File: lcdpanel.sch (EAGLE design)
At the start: 28 parts, among them CON1 AVRISP-NEWSYMBOL-ML6, J1 CHARLCD-LONG, SW1 PUSHSW, SW2 PUSHSW, SW3 PUSHSW, SW4 PUSHSW, U1 ATTINY2313P

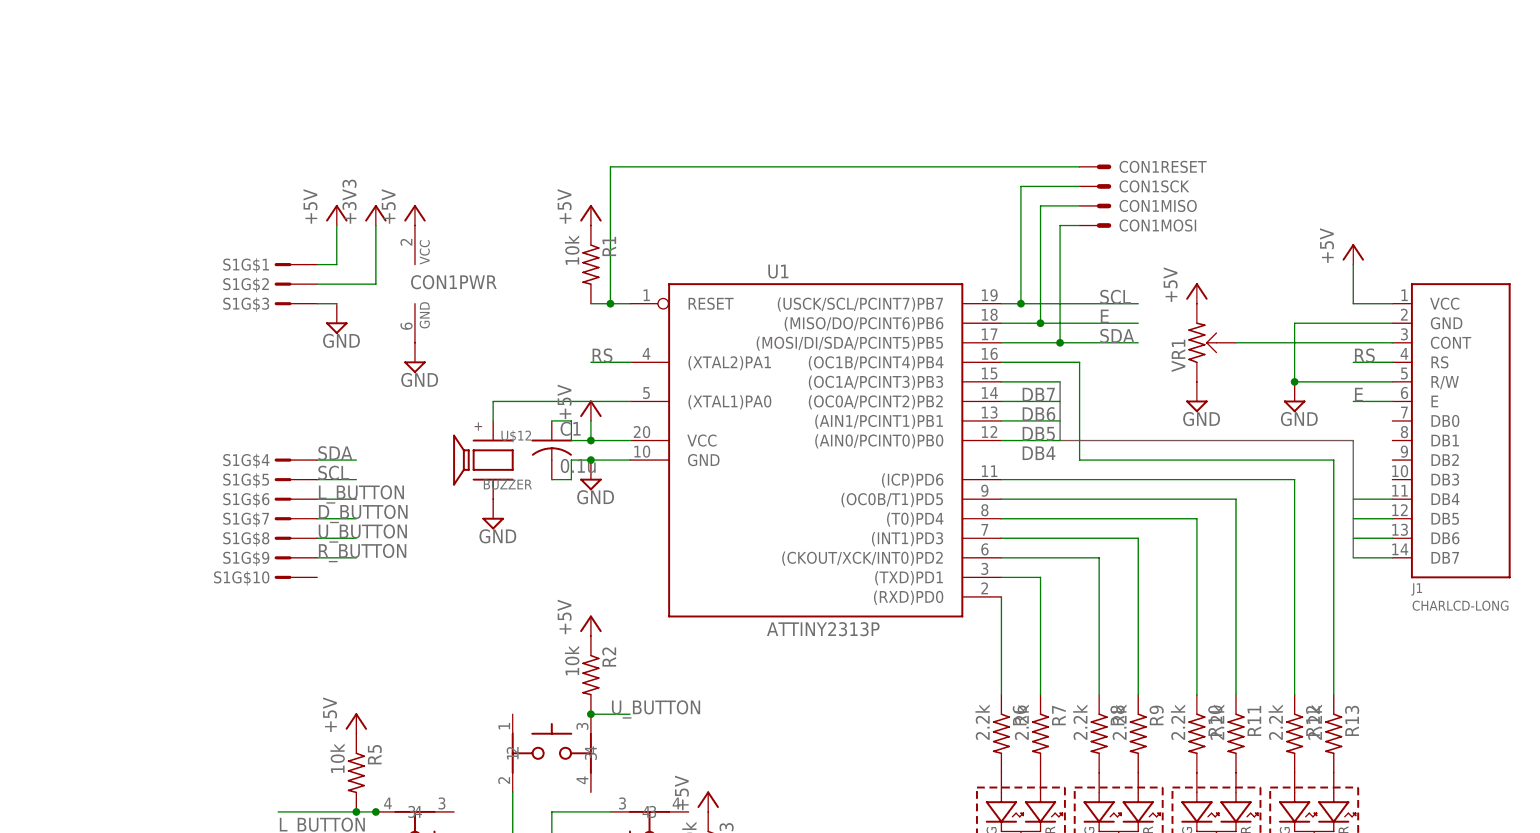
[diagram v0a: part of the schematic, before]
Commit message: added top board (ontheway)
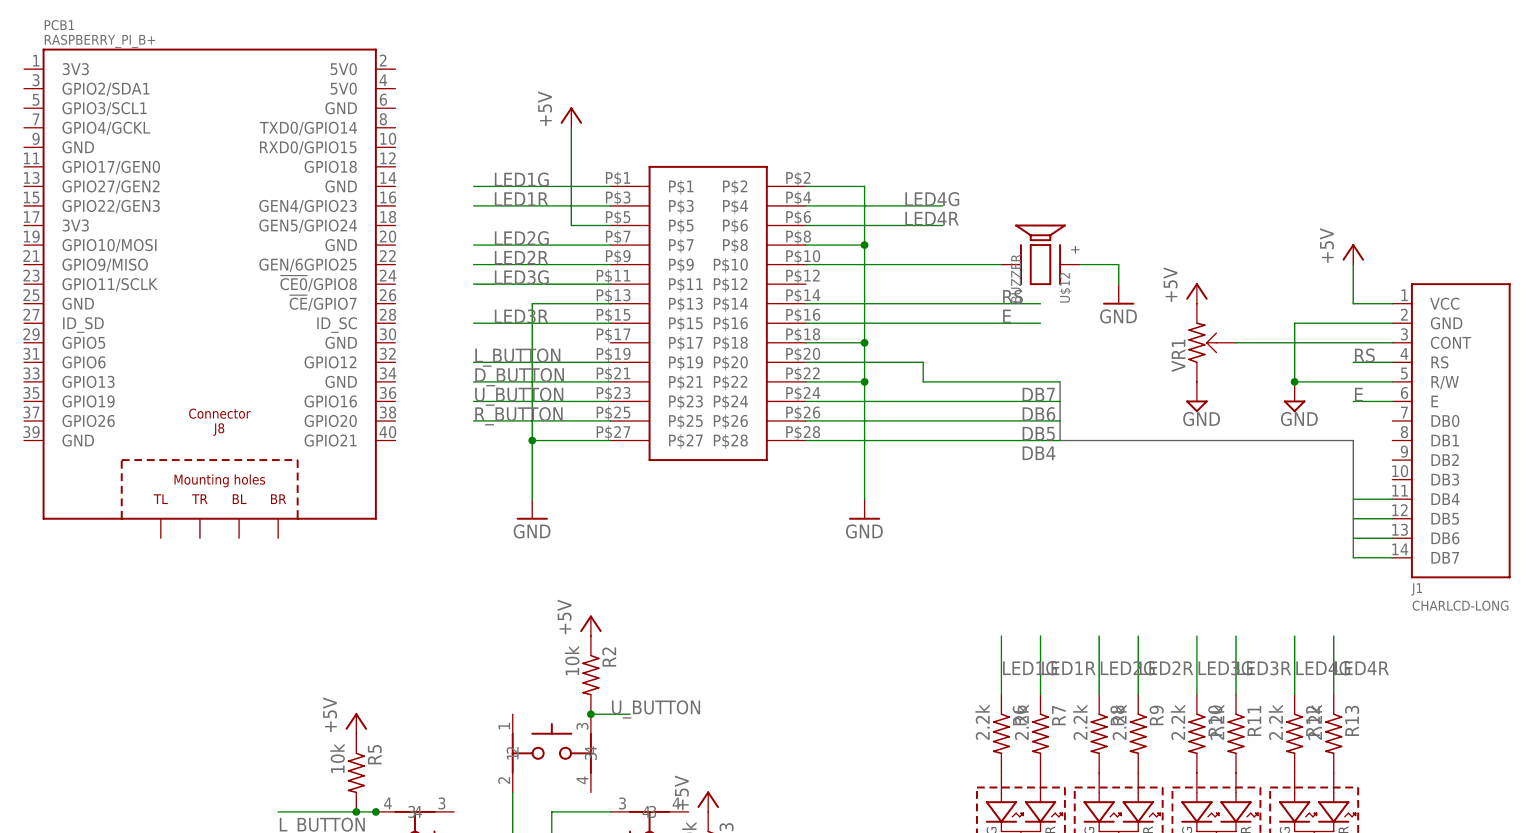
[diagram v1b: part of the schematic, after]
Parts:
- removed C1: 0.1u, Passive_Robotech:C-2012
- removed CON1: AVRISP-NEWSYMBOL-ML6, Connector_Robotech:AVRISP-NEWSYMBOL-ML6
- removed R1: 10k, Passive_Robotech:R-1608
- removed S1: 10B-PH, con-jst:10B-PH
- removed U1: ATTINY2313P, MicroControler_Robotech:ATTINY2313P
- added PCB1: RASPBERRY_PI_B+, RASPBERRY_PI_Bplus:RASPBERRY_PI_B+
- added U$13: CON_14X2, pizaid:CON_14X2
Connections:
- removed net +3V3: S1G$2.1
- removed net N$12: R6.1, U1.(RXD)PD0
- removed net N$13: R7.1, U1.(TXD)PD1
- removed net N$14: R8.1, U1.(CKOUT/XCK/INT0)PD2
- removed net N$15: R9.1, U1.(INT1)PD3
- removed net N$16: R10.1, U1.(T0)PD4
- removed net N$17: R11.1, U1.(OC0B/T1)PD5
- removed net N$18: R12.1, U1.(ICP)PD6
- removed net N$19: R13.1, U1.(OC1B/PCINT4)PB4
- removed net N$20: U$12.+, U1.(XTAL1)PA0
- removed net SCL: CON1SCK.S, S1G$5.1, U1.(USCK/SCL/PCINT7)PB7
- removed net SDA: CON1MOSI.S, S1G$4.1, U1.(MOSI/DI/SDA/PCINT5)PB5
- new net LED1G: R6.1
- net +5V: now also U$13.P$5; no longer C1.1, CON1PWR.VCC, R1.1, S1G$1.1, U1.VCC
- net DB4: now also U$13.P$28; no longer U1.(AIN0/PCINT0)PB0
- net DB5: now also U$13.P$26; no longer U1.(AIN1/PCINT1)PB1
- net DB6: now also U$13.P$24; no longer U1.(OC0A/PCINT2)PB2
- net DB7: now also U$13.P$20; no longer U1.(OC1A/PCINT3)PB3
- net D_BUTTON: no longer S1G$7.1
- net E: now also U$13.P$16; no longer CON1MISO.S, U1.(MISO/DO/PCINT6)PB6
- net GND: now also U$12.+, U$13.P$13, U$13.P$18, U$13.P$2, U$13.P$22, U$13.P$27, U$13.P$8; no longer C1.2, CON1PWR.GND, S1G$3.1, U$12.-, U1.GND
- net L_BUTTON: no longer S1G$6.1
- net N$1: now also U$12.-, U$13.P$10; no longer CON1RESET.S, R1.2, U1.RESET
- net RS: now also U$13.P$14; no longer U1.(XTAL2)PA1
- net R_BUTTON: no longer S1G$9.1
- net U_BUTTON: no longer S1G$8.1
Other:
- moved on the sheet: U$12

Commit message: continuing placement.....................
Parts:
- added U$11, U$2, U$3, U$4: B2P-VH, pizaid:B2P-VH
- added U$14: CON_14X2, pizaid:CON_14X2
- added X1: DCJACK-MJ179P-R, kamiki-dcjack:DCJACK-MJ179P-R
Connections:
- new net 5V0@2: U$11G$1.1, U$14.P$19, U$14.P$20, U$14.P$21, U$14.P$22, U$14.P$23, U$4G$1.1
- new net JNET: U$14.P$10, U$14.P$11, U$14.P$12, U$14.P$13, U$14.P$9, U$2G$1.1, U$3G$1.1
- new net N$13: U$14.P$5, U$14.P$6, U$14.P$7, U$14.P$8, X1.1
- new net N$15: U$14.P$14, U$14.P$15, U$14.P$16, U$14.P$17, U$14.P$18, U$2G$2.1, U$3G$2.1
- new net N$16: U$11G$2.1, U$14.P$24, U$14.P$25, U$14.P$26, U$14.P$27, U$14.P$28, U$4G$2.1
- new net N$18: U$14.P$2, U$14.P$4
- new net N$19: U$14.P$1, U$14.P$3
- net GND: now also X1.2, X1.3

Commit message: airwireが表示されないくてよくわかんない
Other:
- moved on the sheet: PCB1
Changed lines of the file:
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@@
 <setting verticaltext="up"/>
 </settings>
-<grid distance="0.05" unitdist="inch" unit="inch" style="lines" multiple="1" display="no" altdistance="0.01" altunitdist="inch" altunit="inch"/>
+<grid distance="0.1" unitdist="inch" unit="inch" style="lines" multiple="1" display="no" altdistance="0.01" altunitdist="inch" altunit="inch"/>
 <layers>
 <layer number="1" name="Top" color="4" fill="1" visible="no" active="no"/>
@@
 <instance part="SUPPLY7" gate="GND" x="12.7" y="-40.64"/>
 <instance part="U$12" gate="G$1" x="86.36" y="48.26" rot="MR90"/>
-<instance part="PCB1" gate="G$1" x="-20.32" y="50.8"/>
+<instance part="PCB1" gate="G$1" x="-55.88" y="43.18"/>
 <instance part="U$13" gate="G$1" x="43.18" y="43.18"/>
 <instance part="GND1" gate="1" x="63.5" y="15.24"/>
@@
 <net name="R_BUTTON" class="0">
 <segment>
+<wire x1="0" y1="27.94" x2="30.48" y2="27.94" width="0.1524" layer="91"/>
+<label x="12.7" y="27.94" size="1.778" layer="95"/>
+<wire x1="0" y1="27.94" x2="0" y2="7.62" width="0.1524" layer="91"/>
+<wire x1="0" y1="7.62" x2="50.8" y2="7.62" width="0.1524" layer="91"/>
+<wire x1="50.8" y1="7.62" x2="50.8" y2="-33.02" width="0.1524" layer="91"/>
 <pinref part="SW3" gate="G$1" pin="2"/>
 <wire x1="40.64" y1="-33.02" x2="43.18" y2="-33.02" width="0.1524" layer="91"/>
 <pinref part="R3" gate="G$1" pin="2"/>
-<wire x1="43.18" y1="-33.02" x2="45.72" y2="-33.02" width="0.1524" layer="91"/>
 <junction x="43.18" y="-33.02"/>
-<label x="45.72" y="-33.02" size="1.778" layer="95"/>
-</segment>
-<segment>
-<wire x1="12.7" y1="27.94" x2="30.48" y2="27.94" width="0.1524" layer="91"/>
-<label x="12.7" y="27.94" size="1.778" layer="95"/>
+<label x="50.8" y="-33.02" size="1.778" layer="95"/>
+<wire x1="50.8" y1="-33.02" x2="43.18" y2="-33.02" width="0.1524" layer="91"/>
 </segment>
 </net>
 <net name="D_BUTTON" class="0">
 <segment>
-<wire x1="12.7" y1="33.02" x2="30.48" y2="33.02" width="0.1524" layer="91"/>
 <label x="12.7" y="33.02" size="1.778" layer="95"/>
-</segment>
-<segment>
+<wire x1="30.48" y1="33.02" x2="-20.32" y2="33.02" width="0.1524" layer="91"/>
+<wire x1="-20.32" y1="33.02" x2="-20.32" y2="-55.88" width="0.1524" layer="91"/>
 <pinref part="SW4" gate="G$1" pin="4"/>
 <wire x1="27.94" y1="-50.8" x2="33.02" y2="-50.8" width="0.1524" layer="91"/>
@@
 <junction x="33.02" y="-50.8"/>
 <label x="35.56" y="-50.8" size="1.778" layer="95"/>
-</segment>
-</net>
-<net name="L_BUTTON" class="0">
-<segment>
-<pinref part="SW2" gate="G$1" pin="4"/>
-<pinref part="R5" gate="G$1" pin="2"/>
-<junction x="0" y="-22.86"/>
-<label x="-12.7" y="-25.4" size="1.778" layer="95"/>
-<wire x1="-2.54" y1="-22.86" x2="-12.7" y2="-22.86" width="0.1524" layer="91"/>
-<junction x="-2.54" y="-22.86"/>
-<wire x1="0" y1="-22.86" x2="-2.54" y2="-22.86" width="0.1524" layer="91"/>
-</segment>
-<segment>
-<wire x1="12.7" y1="35.56" x2="30.48" y2="35.56" width="0.1524" layer="91"/>
-<label x="12.7" y="35.56" size="1.778" layer="95"/>
+<wire x1="-20.32" y1="-55.88" x2="35.56" y2="-55.88" width="0.1524" layer="91"/>
+<wire x1="35.56" y1="-55.88" x2="35.56" y2="-50.8" width="0.1524" layer="91"/>
 </segment>
 </net>
@@
 <segment>
 <pinref part="SW1" gate="G$1" pin="3"/>
-<wire x1="27.94" y1="-10.16" x2="33.02" y2="-10.16" width="0.1524" layer="91"/>
 <pinref part="R2" gate="G$1" pin="2"/>
 <junction x="27.94" y="-10.16"/>
 <label x="30.48" y="-10.16" size="1.778" layer="95"/>
-</segment>
-<segment>
-<wire x1="12.7" y1="30.48" x2="30.48" y2="30.48" width="0.1524" layer="91"/>
+<wire x1="27.94" y1="-10.16" x2="33.02" y2="-10.16" width="0.1524" layer="91"/>
+<wire x1="33.02" y1="-10.16" x2="33.02" y2="5.08" width="0.1524" layer="91"/>
+<wire x1="33.02" y1="5.08" x2="-2.54" y2="5.08" width="0.1524" layer="91"/>
+<wire x1="-2.54" y1="5.08" x2="-2.54" y2="30.48" width="0.1524" layer="91"/>
+<wire x1="-2.54" y1="30.48" x2="30.48" y2="30.48" width="0.1524" layer="91"/>
 <label x="12.7" y="30.48" size="1.778" layer="95"/>
 </segment>
@@
 </segment>
 </net>
+<net name="L_BUTTON" class="0">
+<segment>
+<label x="12.7" y="35.56" size="1.778" layer="95"/>
+<wire x1="30.48" y1="35.56" x2="-22.86" y2="35.56" width="0.1524" layer="91"/>
+<wire x1="-22.86" y1="35.56" x2="-22.86" y2="-22.86" width="0.1524" layer="91"/>
+<pinref part="SW2" gate="G$1" pin="4"/>
+<pinref part="R5" gate="G$1" pin="2"/>
+<junction x="0" y="-22.86"/>
+<label x="-12.7" y="-25.4" size="1.778" layer="95"/>
+<junction x="-2.54" y="-22.86"/>
+<wire x1="0" y1="-22.86" x2="-2.54" y2="-22.86" width="0.1524" layer="91"/>
+<wire x1="-22.86" y1="-22.86" x2="-2.54" y2="-22.86" width="0.1524" layer="91"/>
+</segment>
+</net>

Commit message: draw stackable lcdpanel, not yet completed
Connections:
- net 5V0@2 renamed N$20
- net JNET renamed N$14
- removed net N$18: U$14.P$2, U$14.P$4
- removed net N$2: SW1.2, SW2.1, SW4.2
- new net LED1R: R7.1, U$13.P$3
- new net LED2G: R8.1, U$13.P$7
- new net LED2R: R9.1, U$13.P$9
- new net LED3G: R10.1, U$13.P$11
- new net LED3R: R11.1, U$13.P$15
- new net LED4G: R12.1, U$13.P$4
- new net LED4R: R13.1, U$13.P$6
- net D_BUTTON: now also U$13.P$21
- net GND: now also PCB1.BL, PCB1.BR, PCB1.TL, PCB1.TR, SW1.2, SW2.1; no longer X1.2, X1.3
- net LED1G: now also U$13.P$1
- net L_BUTTON: now also U$13.P$19
- net N$19: now also U$14.P$2, U$14.P$4, X1.2, X1.3
- net R_BUTTON: now also U$13.P$25
- net U_BUTTON: now also U$13.P$23
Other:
- moved on the sheet: R10, R11, R12, R13, R6, R7, R8, R9

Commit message: completed rev1
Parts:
- added C1, C2: (no value), rcl:C-EUC0603
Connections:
- net +5V: now also C1.1, C2.1
- net GND: now also C1.2, C2.2
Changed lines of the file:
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@@
 </classes>
 <parts>
-<part name="J1" library="pizaid" deviceset="CHARLCD" device="-LONG"/>
 <part name="SW1" library="Passive_Robotech" deviceset="PUSHSW" device=""/>
 <part name="SW2" library="Passive_Robotech" deviceset="PUSHSW" device=""/>
@@
 <part name="X1" library="kamiki-dcjack" deviceset="DCJACK" device="-MJ179P-R"/>
 <part name="GND4" library="supply1" deviceset="GND" device=""/>
+<part name="C1" library="rcl" deviceset="C-EU" device="C0603"/>
+<part name="C2" library="rcl" deviceset="C-EU" device="C0603"/>
+<part name="GND5" library="supply1" deviceset="GND" device=""/>
+<part name="J1" library="pizaid" deviceset="CHARLCD" device="-LONG"/>
+<part name="U$15" library="Supply_Robotech" deviceset="+5V" device=""/>
 </parts>
 <sheets>
@@
 </plain>
 <instances>
-<instance part="J1" gate="G$1" x="134.62" y="25.4"/>
 <instance part="SW1" gate="G$1" x="22.86" y="-15.24"/>
 <instance part="SW2" gate="G$1" x="5.08" y="-27.94" rot="MR90"/>
@@
 <instance part="U$7" gate="1" x="43.18" y="-22.86"/>
 <instance part="U$8" gate="1" x="33.02" y="-40.64"/>
-<instance part="U$9" gate="1" x="127" y="48.26"/>
+<instance part="U$9" gate="1" x="127" y="60.96"/>
 <instance part="SUPPLY3" gate="GND" x="119.38" y="30.48"/>
 <instance part="SUPPLY4" gate="GND" x="106.68" y="30.48"/>
@@
 <instance part="X1" gate="G$1" x="182.88" y="35.56"/>
 <instance part="GND4" gate="1" x="-63.5" y="-5.08"/>
+<instance part="C1" gate="G$1" x="119.38" y="48.26"/>
+<instance part="C2" gate="G$1" x="58.42" y="-15.24"/>
+<instance part="GND5" gate="1" x="58.42" y="-25.4"/>
+<instance part="J1" gate="G$1" x="134.62" y="25.4"/>
+<instance part="U$15" gate="1" x="58.42" y="-10.16"/>
 </instances>
 <busses>
@@
 <segment>
 <pinref part="U$9" gate="1" pin="+5V"/>
+<wire x1="127" y1="60.96" x2="127" y2="53.34" width="0.1524" layer="91"/>
+<wire x1="127" y1="53.34" x2="127" y2="43.18" width="0.1524" layer="91"/>
+<wire x1="127" y1="43.18" x2="132.08" y2="43.18" width="0.1524" layer="91"/>
+<pinref part="C1" gate="G$1" pin="1"/>
+<wire x1="119.38" y1="50.8" x2="119.38" y2="53.34" width="0.1524" layer="91"/>
+<wire x1="119.38" y1="53.34" x2="127" y2="53.34" width="0.1524" layer="91"/>
+<junction x="127" y="53.34"/>
 <pinref part="J1" gate="G$1" pin="VCC"/>
-<wire x1="127" y1="48.26" x2="127" y2="43.18" width="0.1524" layer="91"/>
-<wire x1="127" y1="43.18" x2="132.08" y2="43.18" width="0.1524" layer="91"/>
 </segment>
 <segment>
@@
 <pinref part="U$1" gate="1" pin="+5V"/>
 </segment>
+<segment>
+<pinref part="C2" gate="G$1" pin="1"/>
+<wire x1="58.42" y1="-10.16" x2="58.42" y2="-12.7" width="0.1524" layer="91"/>
+<pinref part="U$15" gate="1" pin="+5V"/>
+</segment>
 </net>
 <net name="GND" class="0">
 <segment>
 <pinref part="SUPPLY3" gate="GND" pin="GND"/>
-<pinref part="J1" gate="G$1" pin="GND"/>
-<pinref part="J1" gate="G$1" pin="R/W"/>
 <wire x1="119.38" y1="33.02" x2="119.38" y2="40.64" width="0.1524" layer="91"/>
 <wire x1="119.38" y1="40.64" x2="132.08" y2="40.64" width="0.1524" layer="91"/>
 <wire x1="132.08" y1="33.02" x2="119.38" y2="33.02" width="0.1524" layer="91"/>
 <junction x="119.38" y="33.02"/>
+<pinref part="C1" gate="G$1" pin="2"/>
+<wire x1="119.38" y1="40.64" x2="119.38" y2="43.18" width="0.1524" layer="91"/>
+<junction x="119.38" y="40.64"/>
+<pinref part="J1" gate="G$1" pin="GND"/>
+<pinref part="J1" gate="G$1" pin="R/W"/>
 </segment>
 <segment>
@@
 <junction x="-58.42" y="0"/>
 </segment>
+<segment>
+<pinref part="GND5" gate="1" pin="GND"/>
+<pinref part="C2" gate="G$1" pin="2"/>
+<wire x1="58.42" y1="-22.86" x2="58.42" y2="-20.32" width="0.1524" layer="91"/>
+</segment>
 </net>
 <net name="DB4" class="0">
 <segment>
+<wire x1="132.08" y1="17.78" x2="127" y2="17.78" width="0.1524" layer="91"/>
 <pinref part="J1" gate="G$1" pin="DB4"/>
-<wire x1="132.08" y1="17.78" x2="127" y2="17.78" width="0.1524" layer="91"/>
 </segment>
 <segment>
@@
 <net name="DB5" class="0">
 <segment>
+<wire x1="132.08" y1="15.24" x2="127" y2="15.24" width="0.1524" layer="91"/>
 <pinref part="J1" gate="G$1" pin="DB5"/>
-<wire x1="132.08" y1="15.24" x2="127" y2="15.24" width="0.1524" layer="91"/>
 </segment>
 <segment>
@@
 <net name="DB6" class="0">
 <segment>
+<wire x1="132.08" y1="12.7" x2="127" y2="12.7" width="0.1524" layer="91"/>
 <pinref part="J1" gate="G$1" pin="DB6"/>
-<wire x1="132.08" y1="12.7" x2="127" y2="12.7" width="0.1524" layer="91"/>
 </segment>
 <segment>
@@
 <net name="DB7" class="0">
 <segment>
+<wire x1="132.08" y1="10.16" x2="127" y2="10.16" width="0.1524" layer="91"/>
 <pinref part="J1" gate="G$1" pin="DB7"/>
-<wire x1="132.08" y1="10.16" x2="127" y2="10.16" width="0.1524" layer="91"/>
 </segment>
 <segment>
@@
 </segment>
 <segment>
-<pinref part="J1" gate="G$1" pin="RS"/>
 <wire x1="132.08" y1="35.56" x2="127" y2="35.56" width="0.1524" layer="91"/>
 <label x="127" y="35.56" size="1.778" layer="95"/>
+<pinref part="J1" gate="G$1" pin="RS"/>
 </segment>
 </net>
@@
 </segment>
 <segment>
-<pinref part="J1" gate="G$1" pin="E"/>
 <wire x1="132.08" y1="30.48" x2="127" y2="30.48" width="0.1524" layer="91"/>
 <label x="127" y="30.48" size="1.778" layer="95"/>
+<pinref part="J1" gate="G$1" pin="E"/>
 </segment>
 </net>
@@
 <segment>
 <pinref part="VR1" gate="G$1" pin="BR"/>
+<wire x1="111.76" y1="38.1" x2="132.08" y2="38.1" width="0.1524" layer="91"/>
 <pinref part="J1" gate="G$1" pin="CONT"/>
-<wire x1="111.76" y1="38.1" x2="132.08" y2="38.1" width="0.1524" layer="91"/>
-</segment>
-</net>
+</segment>
+</net>
